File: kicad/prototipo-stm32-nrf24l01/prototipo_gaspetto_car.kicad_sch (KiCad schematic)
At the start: 11 parts, among them J1 Conn_01x07_Pin - TEST POINT, M1 Motor_DC, M2 Motor_DC, Q1 BC548, U1 YAAJ_BluePill_Part_Like_SWD_B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, U2 nRF24L01+, U3 L9110-M2, U4 L9110-M1, U5 5 to 3.3v

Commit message: car: motor and radio
- We receive radio commands and execute them. I have some issues
  controlling DC motors, will try to restructure a bit and add
  a PID controller.
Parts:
- M1: value Motor_DC -> Motor_DC Right
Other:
- note added: "vista PCB lado componentes, conector USB uC arriba"
- note removed: "vista PCB lado componentes, conector USB arriba"
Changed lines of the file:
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@@
 		)
 	)
-	(text "vista PCB lado componentes, conector USB arriba\n"
+	(text "vista PCB lado componentes, conector USB uC arriba\n"
 		(exclude_from_sim no)
 		(at 286.766 226.314 0)
@@
 		(on_board yes)
 		(dnp no)
-		(fields_autoplaced yes)
 		(property "Reference" "M1"
 			(at 266.7 167.64 90)
@@
 			)
 		)
-		(property "Value" "Motor_DC"
+		(property "Value" "Motor_DC Right"
 			(at 266.7 170.18 90)
 			(effects

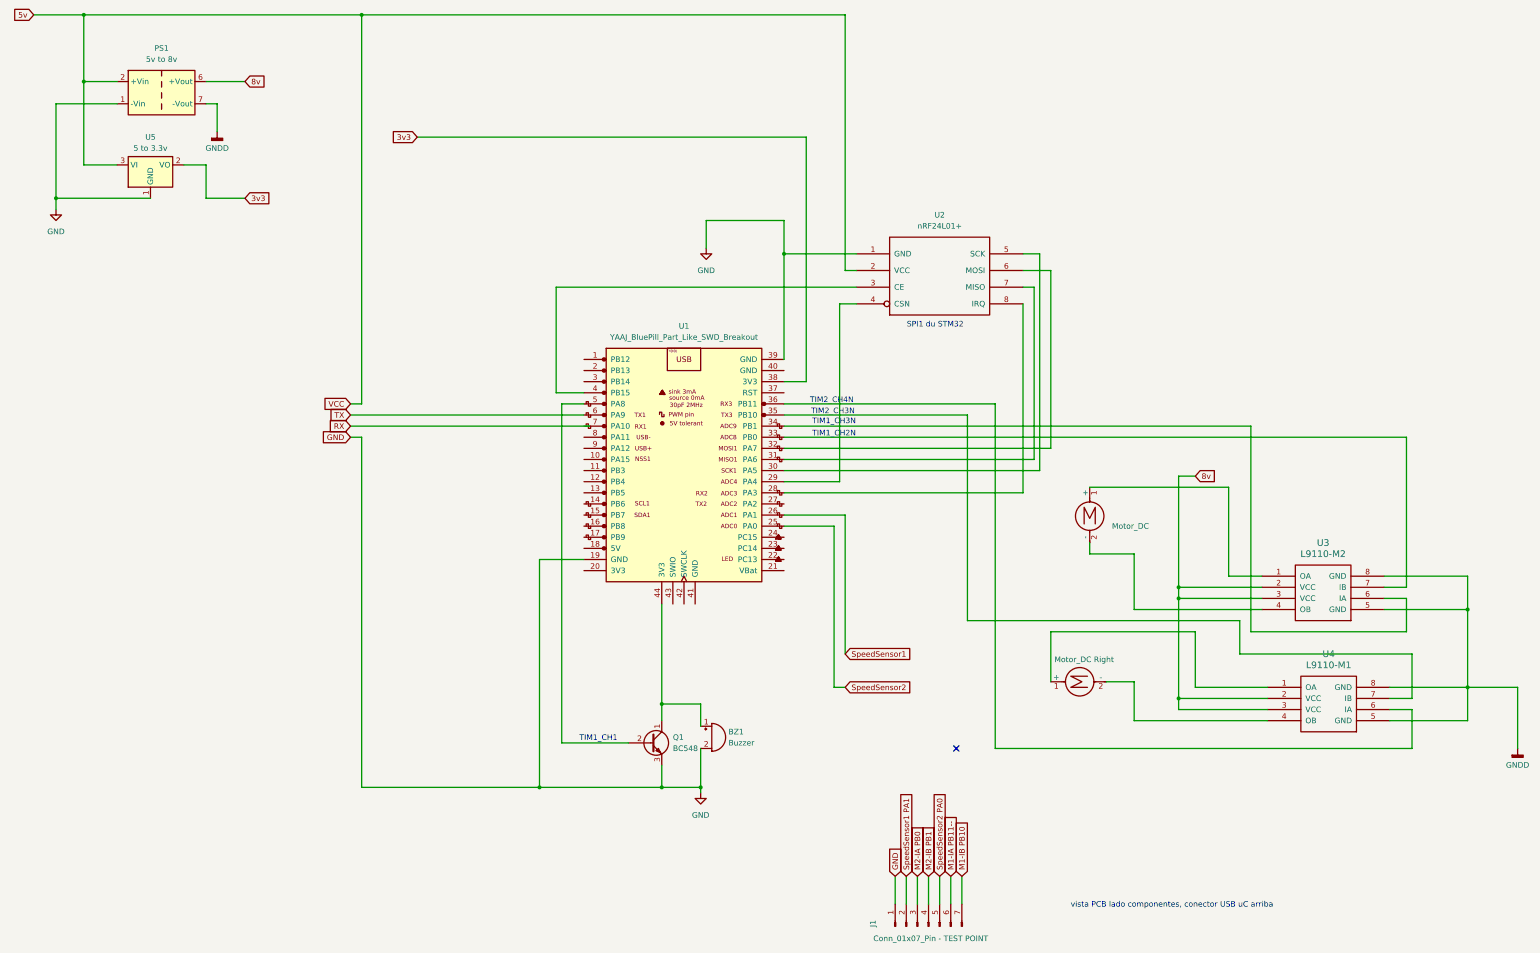
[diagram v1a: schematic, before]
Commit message: car: motor and radio
- We receive radio commands and execute them. I have some issues
  controlling DC motors, will try to restructure a bit and add
  a PID controller.
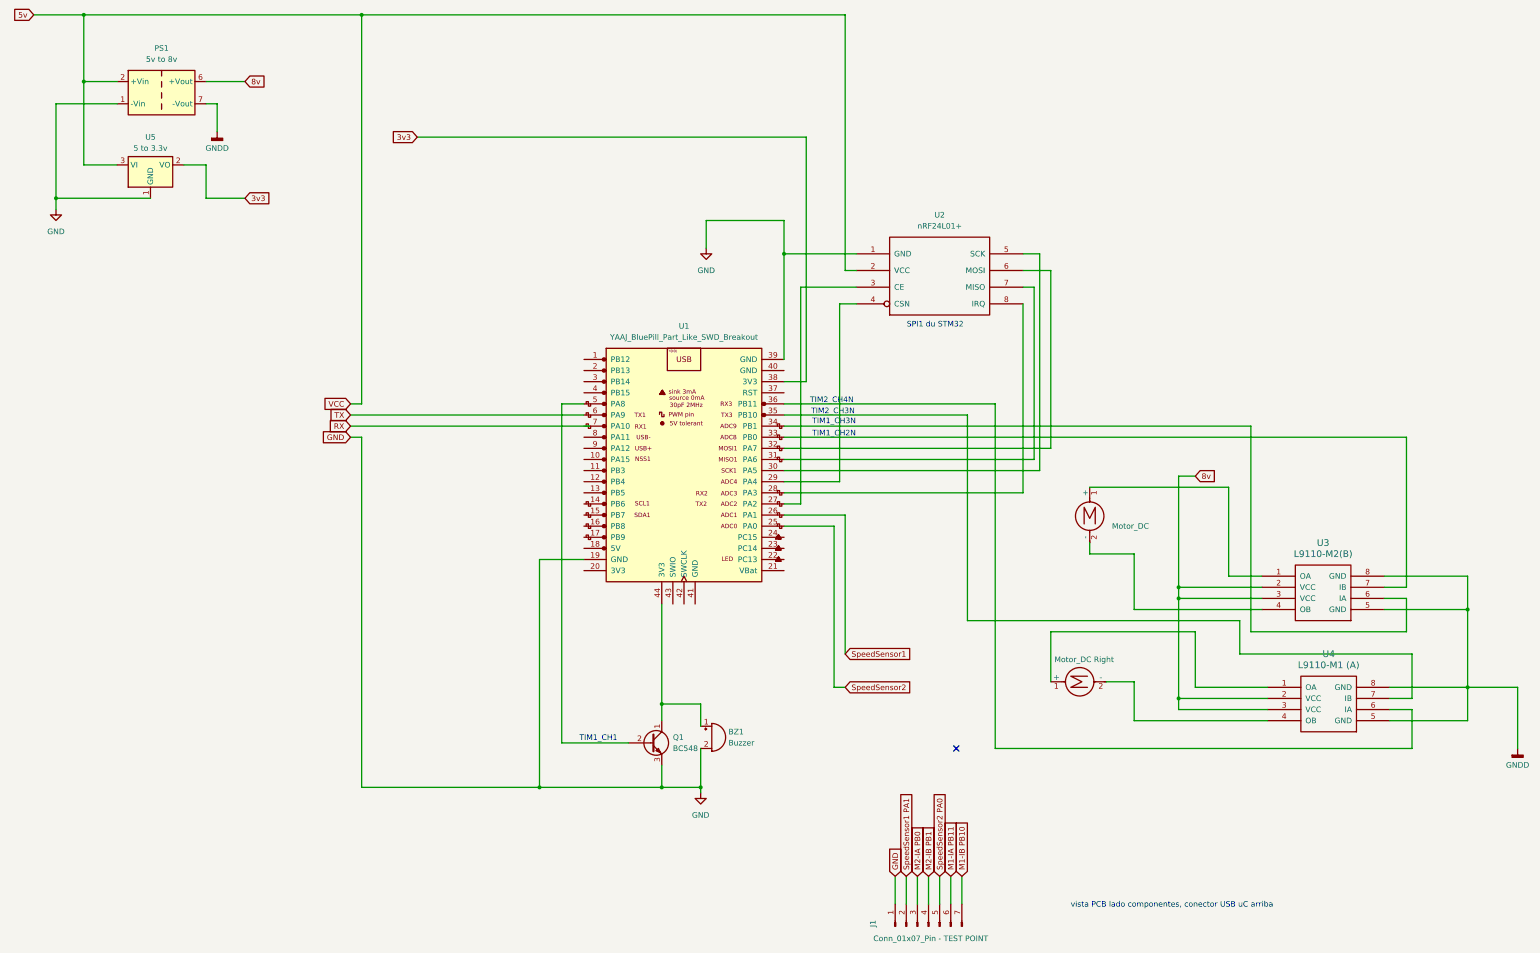
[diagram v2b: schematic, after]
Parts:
- U3: value L9110-M2 -> L9110-M2(B)
- U4: value L9110-M1 -> L9110-M1 (A)
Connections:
- net at U1.27 (PA2): now also U2.3 (CE)
- net at U1.4 (PB15): no longer U2.3 (CE)
- net M1-IA PB11-- renamed M1-IA PB11
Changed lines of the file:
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@@
-	(wire
-		(pts
-			(xy 146.05 109.22) (xy 152.4 109.22)
-		)
-		(stroke
-			(width 0)
-			(type default)
-		)
-	)
 	(wire
 		(pts
@@
 	(wire
 		(pts
+			(xy 201.93 134.62) (xy 201.93 85.09)
+		)
+		(stroke
+			(width 0)
+			(type default)
+		)
+	)
+	(wire
+		(pts
 			(xy 114.3 50.8) (xy 203.2 50.8)
 		)
@@
 	(wire
 		(pts
-			(xy 214.63 85.09) (xy 146.05 85.09)
+			(xy 214.63 85.09) (xy 201.93 85.09)
 		)
 		(stroke
@@
 	(wire
 		(pts
+			(xy 198.12 134.62) (xy 201.93 134.62)
+		)
+		(stroke
+			(width 0)
+			(type default)
+		)
+	)
+	(wire
+		(pts
 			(xy 341.63 168.91) (xy 302.26 168.91)
 		)
@@
 		(pts
 			(xy 354.33 184.15) (xy 336.55 184.15)
-		)
-		(stroke
-			(width 0)
-			(type default)
-		)
-	)
-	(wire
-		(pts
-			(xy 146.05 85.09) (xy 146.05 109.22)
 		)
 		(stroke
@@
 		)
 	)
-	(global_label "M1-IA PB11--"
+	(global_label "M1-IA PB11"
 		(shape input)
 		(at 236.22 219.71 90)
@@
 		)
 		(property "Intersheetrefs" "${INTERSHEET_REFS}"
-			(at 236.22 201.7267 90)
+			(at 236.22 204.8715 90)
 			(effects
 				(font
@@
 			)
 		)
-		(property "Value" "L9110-M2"
+		(property "Value" "L9110-M2(B)"
 			(at 321.31 146.05 0)
 			(effects
@@
 			)
 		)
-		(property "Value" "L9110-M1"
+		(property "Value" "L9110-M1 (A)"
 			(at 322.58 171.45 0)
 			(effects
